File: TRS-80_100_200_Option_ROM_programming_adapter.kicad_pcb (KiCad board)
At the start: 2 copper layers, 17.8 x 48.3 mm, 7 parts, among them J1 Model 100/102/200 Option ROM 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, U1 27C256 pinout to programmer

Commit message: kicad 6
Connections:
- net /ALE~CE renamed /ALE~{CE}
- net /~CE renamed /~{CE}
- net /~OE renamed /~{OE}
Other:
- net class Default removed
- board text added: "~{CE}"
- board text removed: "~CE"

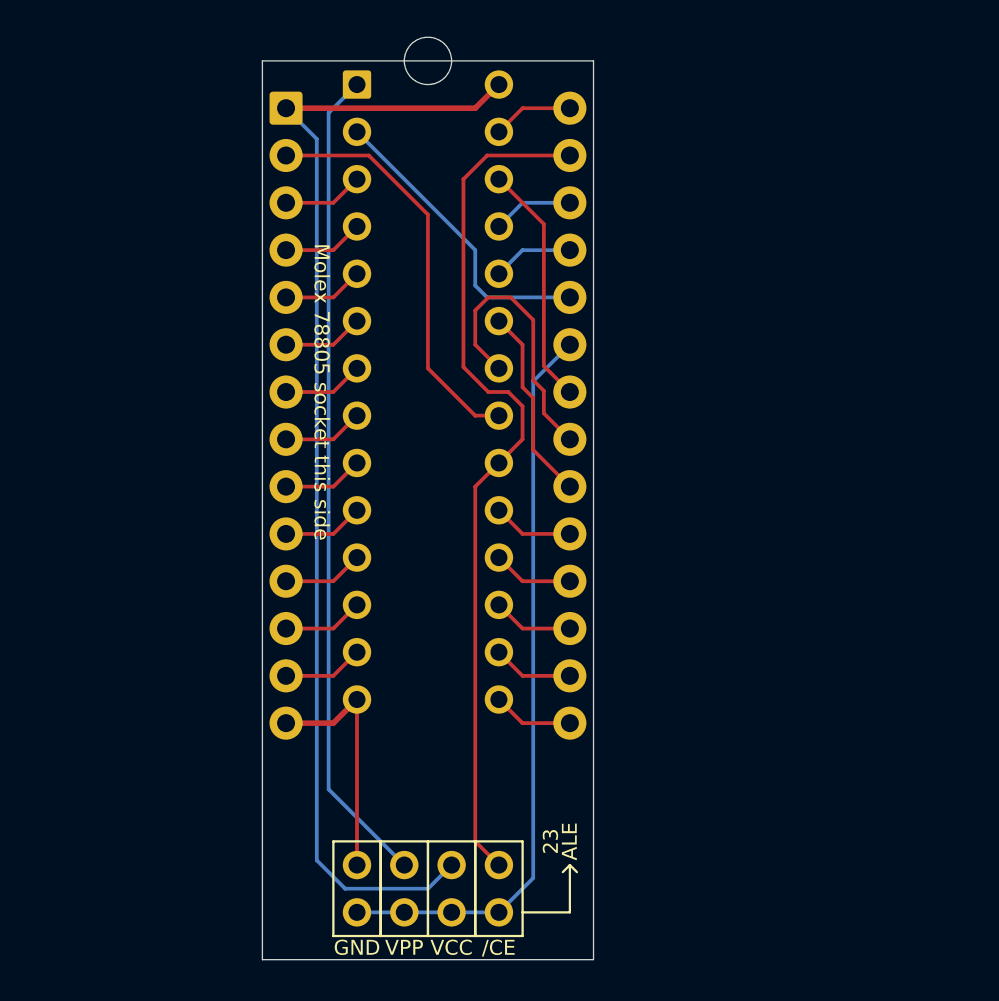
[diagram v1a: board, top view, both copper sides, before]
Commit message: m100 optrom reader outline, silk, sch
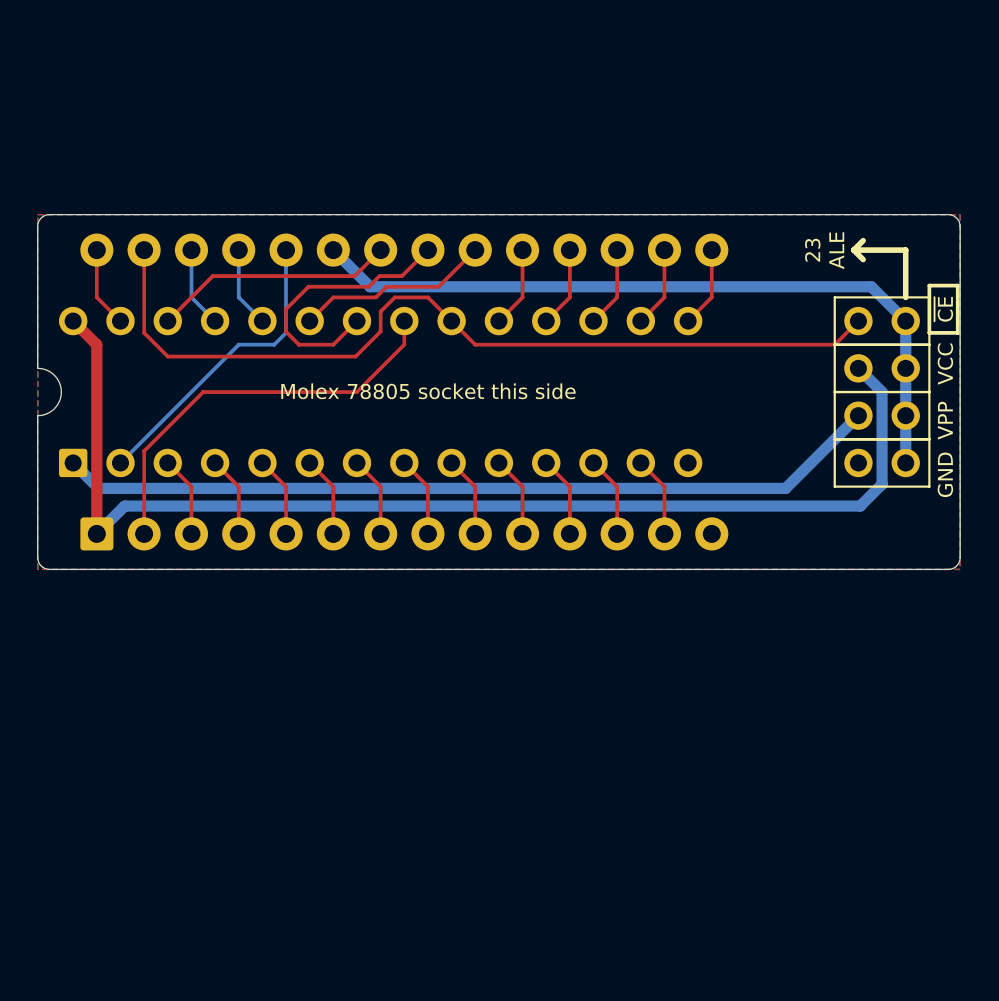
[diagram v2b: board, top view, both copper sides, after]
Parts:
- removed polarity notch: NPTH_0.1, 000_LOCAL:NPTH_0.1
- JP4: value /CE -> ~{CE}
- moved JP4 38.5 mm to (175.7, 96.2), turned to -90 degrees
- moved JP1 38.1 mm to (175.7, 103.8), turned to -90 degrees
- moved JP3 38.1 mm to (175.7, 98.7), turned to -90 degrees
- moved JP2 37.9 mm to (175.7, 101.3), turned to -90 degrees
- moved J1 2.54 mm to (147.5, 100.0), turned to 90 degrees
- moved J2 1.80 mm to (148.7, 100.0), turned to 90 degrees
- renumbered U1 to J1, J1 to J2
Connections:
- net /ALE~{CE} renamed /ALE/~{CE}
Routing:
- net GND: track 13.2 -> 0.00 mm
- net VCC: track 61.4 -> 62.0 mm
- added copper zone on B.Cu, net GND
- added copper zone on F.Cu, net GND
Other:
- board size 17.8 x 48.3 mm -> 49.5 x 19.1 mm
- board text added: "23 ALE"
- board text removed: "23"

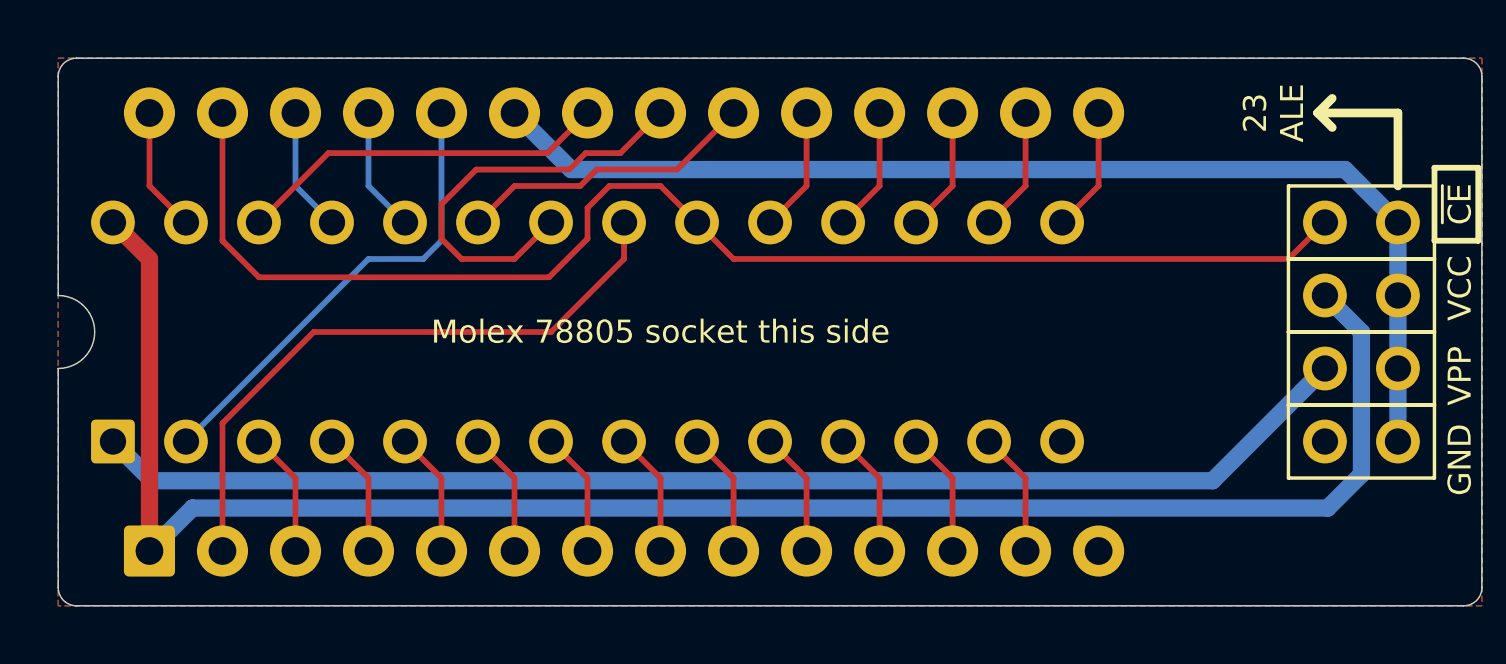
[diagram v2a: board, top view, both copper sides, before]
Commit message: flexrom 102 & 200 accept eeprom or fram
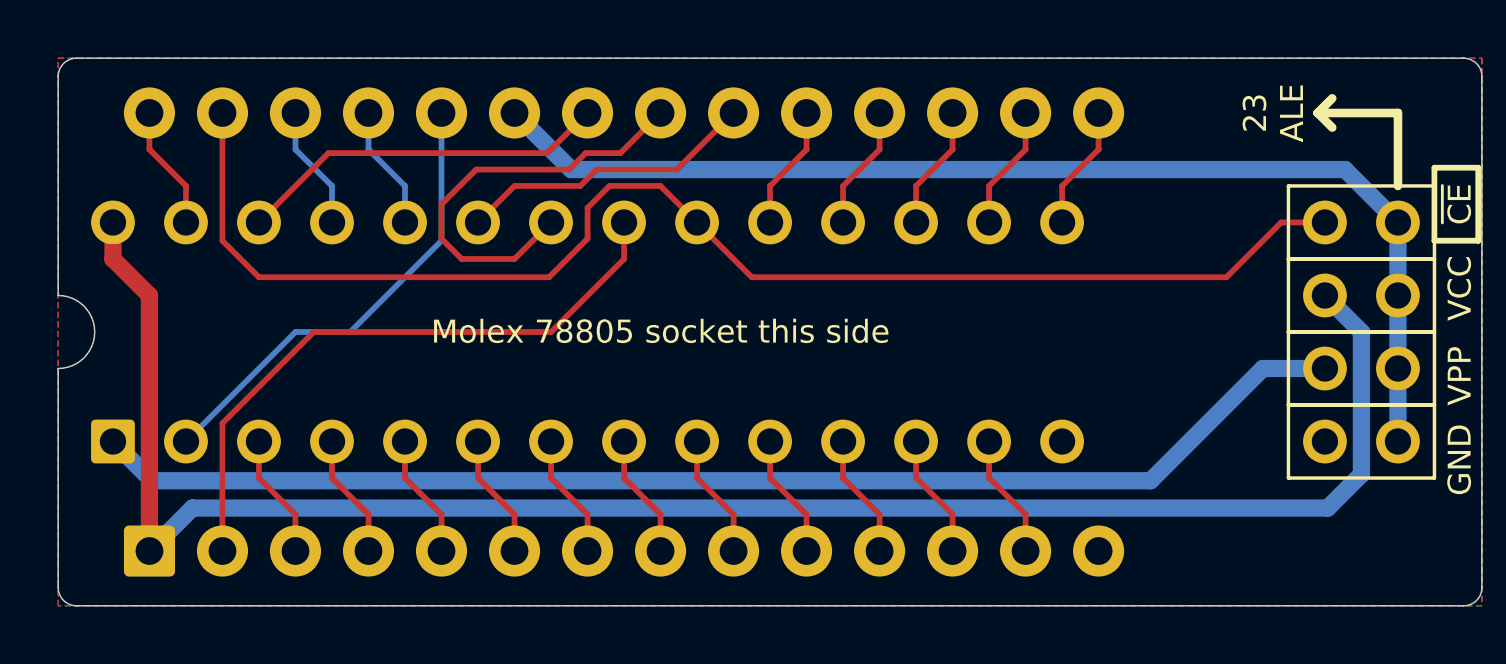
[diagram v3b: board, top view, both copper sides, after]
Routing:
- net /~{CE}: track 46.8 -> 47.4 mm
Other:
- board text added: "${COMMENT2}"
- board text added: "${TITLE}"
- board text removed: "TRS-80 Model 100/102/200 Option ROM Reader"
- board text removed: "github.com/bkw777/aDIPters"
